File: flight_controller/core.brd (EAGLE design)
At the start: 96 x 48 mm, 119 parts, among them J1 M02, J10 M02, J11 M03, J12 M02, J13 M02, J14 M02, J15 M03, J16 M03, J17 M03, J18 M04, J19 M04, J2 M02, J20 M03, J21 M04, J3 M02, J4 M03, J5 M02, J6 M02, J7 M02, J8 M02, J9 M03, Q1 EM6K1, Q2 EM6K1, Q3 EM6K1, Q4 EM6K1, Q5 EM6K1, Q6 EM6K1, Q7 MOSFET-PCHANNEL-AON6407, U1 STM32F405, U2 MEAS-MS5611, U3 MPU-9250-QFN-24-NP, U4 MIC5219 3.3V, U5 USD-SOCKETNEW, Y1 16MHz

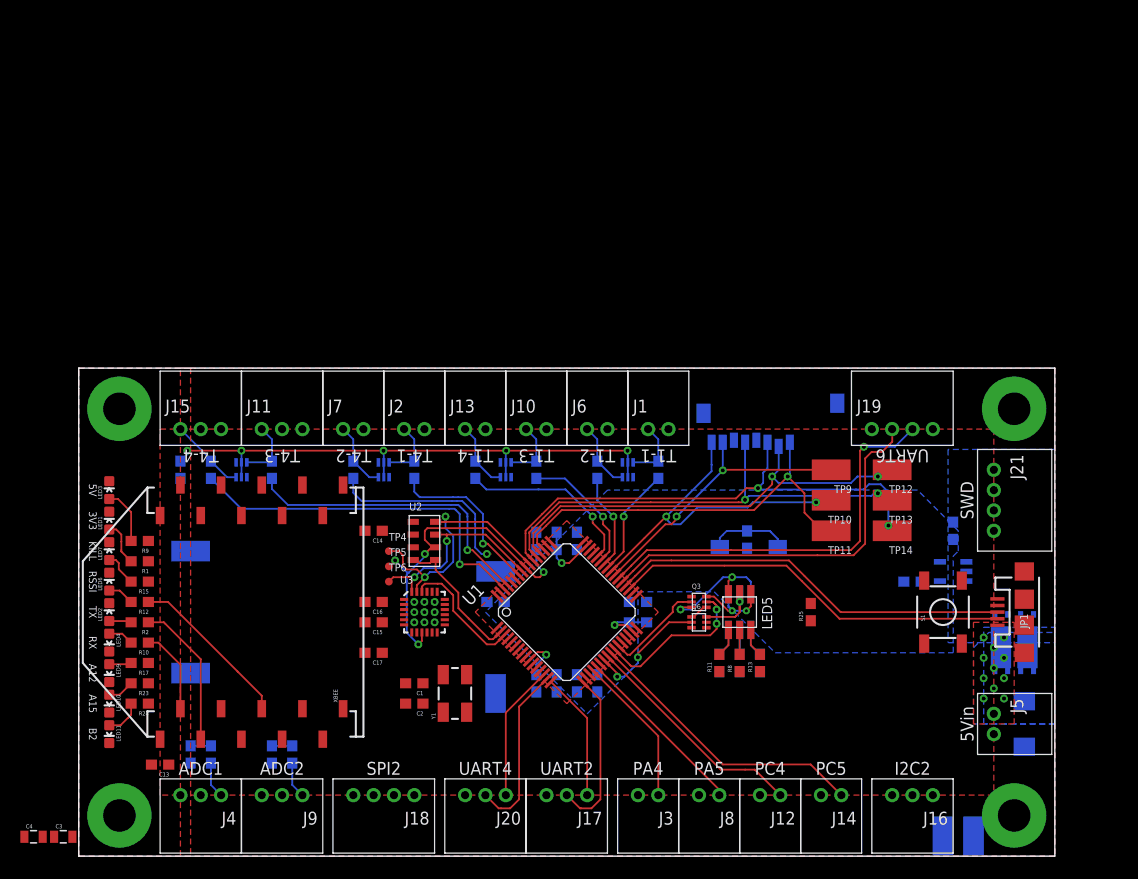
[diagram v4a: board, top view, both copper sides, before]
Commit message: Layout 70% done with new 8MHz crystal.
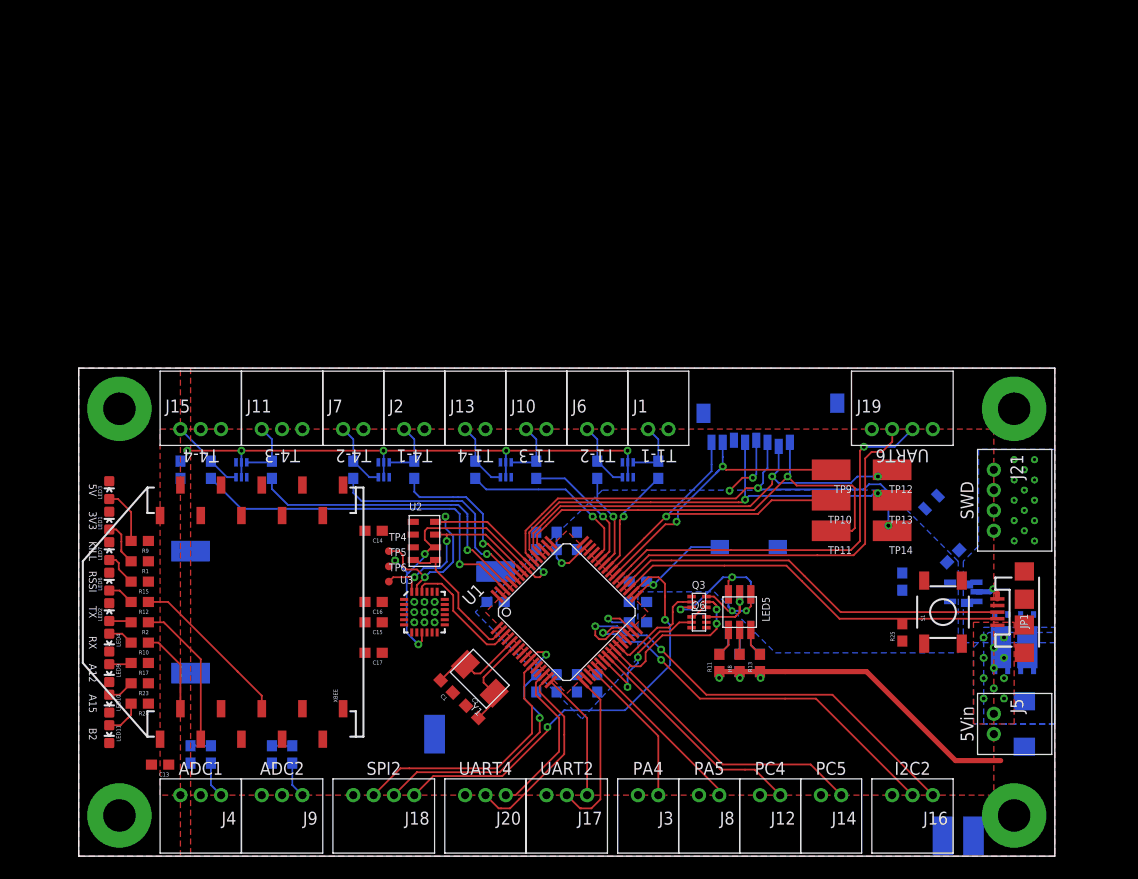
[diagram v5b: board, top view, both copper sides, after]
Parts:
- C4: value 10uF -> 1nF; device OSURC_Passives:0805 -> OSURC_Passives:0603
- C5: value 1nF -> 10uF; device OSURC_Passives:0603 -> OSURC_Passives:0805
- Y1: value 16MHz -> 8MHz; device SparkFun-FreqCtrl:CRYSTAL-SMD-5X3 -> OSURC_FreqCtrl:CX532
- moved C3 92.0 mm to (87.4, 25.8), flipped to the bottom, turned to 90 degrees
- moved C4 89.1 mm to (81.0, 27.0), flipped to the bottom, turned to 270 degrees
- moved R34 11.5 mm to (55.0, 27.0), turned to 0 degrees
- moved R25 9.22 mm to (81.0, 22.0)
- moved C5 8.03 mm to (83.9, 34.8), turned to 315 degrees
- moved TP15 7.21 mm to (35.0, 12.0)
- moved C2 5.75 mm to (38.7, 14.2), turned to 315 degrees
- moved C1 3.21 mm to (36.2, 16.7), turned to 135 degrees
- moved Y1 2.84 mm to (39.4, 17.4), turned to 135 degrees
- moved C6 2.50 mm to (86.0, 29.5), turned to 315 degrees
- moved U4 2.24 mm to (87.0, 26.0)
- turned C12 to 0 degrees
- turned C9 to 0 degrees
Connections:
- net 3.3V: now also C5.2; no longer C4.2
- net MIC-BP: now also C4.2; no longer C5.2
- net OSC-IN: now also Y1.2; no longer Y1.3
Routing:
- net I2C2-SCL: track 0.00 -> 44.7 mm, vias 0 -> 2
- net SPI2-SCK: track 0.00 -> 42.9 mm, vias 0 -> 2
- net I2C2-SDA: track 0.00 -> 40.2 mm, vias 0 -> 2
- net 5V: track 0.00 -> 31.3 mm, vias 0 -> 14
- net SPI2-MOSI: track 0.00 -> 25.6 mm
- net SPI2-MISO: track 4.45 -> 28.1 mm, vias 1 -> 2
- net OSC-OUT: track 0.00 -> 9.45 mm
- net OSC-IN: track 0.00 -> 9.25 mm
- net 3.3V: track 0.00 -> 6.64 mm, vias 9 -> 11
- net SDIO-D2: track 39.8 -> 45.6 mm
- net TIM4-CH2: track 19.4 -> 23.1 mm
- net USD-CD: track 8.01 -> 11.1 mm, vias 0 -> 1
- net GND: track 1.85 -> 4.75 mm, vias 0 -> 1
- net UART4-TX: track 13.4 -> 15.9 mm
- net UART4-RX: track 17.3 -> 19.3 mm
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
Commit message: FC layout 90% done.
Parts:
- removed TP15: TEST-POINT-KEYSTONE-5019, OSURC_Passives:PAD.15X.08
- TP1, TP7, TP8: value TEST-POINT-KEYSTONE-5019 -> TEST-POINT-PAD.03C; device OSURC_Passives:PAD.15X.08 -> OSURC_Passives:PAD-.03C
- moved TP8 22.7 mm to (88.0, 24.5), flipped to the top, turned to 0 degrees
- moved TP7 21.0 mm to (88.0, 23.0), flipped to the top, turned to 0 degrees
- moved TP9 20.6 mm to (58.0, 51.0), turned to 0 degrees
- moved TP11 20.6 mm to (66.0, 51.0), turned to 0 degrees
- moved TP10 20.0 mm to (62.0, 51.0), turned to 0 degrees
- moved TP14 19.1 mm to (78.0, 51.0), turned to 0 degrees
- moved TP13 17.1 mm to (74.0, 51.0), turned to 0 degrees
- moved TP12 16.4 mm to (70.0, 51.0), turned to 0 degrees
- moved S1 11.0 mm to (84.0, 35.0), turned to 0 degrees
- moved R25 9.85 mm to (85.0, 31.0), turned to 0 degrees
- moved C4 8.25 mm to (89.0, 29.0), flipped to the top, turned to 90 degrees
- moved C5 6.90 mm to (85.0, 28.0), turned to 90 degrees
- moved U4 5.83 mm to (92.0, 29.0)
- moved C3 4.84 mm to (91.0, 29.0), flipped to the top
- moved TP1 4.34 mm to (44.2, 25.1)
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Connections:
- net OSC-IN: no longer TP15.1
- net VIN: now also Q7.10, Q7.9
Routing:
- net PB2: track 0.00 -> 60.6 mm, vias 0 -> 6
- net PA12: track 0.00 -> 55.7 mm, vias 0 -> 4
- net PA15: track 0.00 -> 52.7 mm, vias 0 -> 4
- net 3.3V: track 6.64 -> 56.2 mm, vias 11 -> 12
- net SWDIO: track 0.00 -> 48.9 mm, vias 0 -> 4
- net SWCLK: track 0.00 -> 48.5 mm, vias 0 -> 4
- net TIM3-CH1-RSSI: track 16.3 -> 64.0 mm, vias 0 -> 5
- net UART2-RX-XBEE: track 24.9 -> 70.4 mm, vias 0 -> 1
- net UART2-TX-XBEE: track 27.1 -> 68.7 mm, vias 0 -> 1
- net ADC1: track 2.00 -> 42.3 mm, vias 0 -> 3
- net ADC2: track 2.00 -> 35.6 mm, vias 0 -> 3
- net GND: track 4.75 -> 25.7 mm, vias 1 -> 32
- net KILL: track 55.1 -> 72.8 mm, vias 5 -> 8
- net SDIO-D1: track 33.6 -> 17.6 mm
- net SDIO-CMD: track 50.1 -> 35.5 mm, vias 2 -> 1
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- added copper zone on layer 1, net MPU9250-REGOUT

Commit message: Resolve all errors and finish routing.
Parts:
- C13: value 100nF -> 10uF; device OSURC_Passives:0603 -> OSURC_Passives:0805
- moved TP9 20.6 mm to (73.5, 37.5)
- moved TP14 15.7 mm to (63.5, 45.0), turned to 90 degrees
- moved TP10 15.6 mm to (73.5, 40.5)
- moved C3 14.1 mm to (93.0, 15.0), turned to 0 degrees
- moved TP13 9.60 mm to (66.5, 45.0), turned to 90 degrees
- moved TP11 8.85 mm to (72.5, 45.0), turned to 90 degrees
- moved TP12 6.02 mm to (69.5, 45.0), turned to 90 degrees
- moved TP1 3.28 mm to (42.0, 27.5)
- moved C13 2.50 mm to (10.5, 9.00)
- moved R25 2.24 mm to (87.0, 32.0), flipped to the bottom, turned to 270 degrees
- moved C4 1.00 mm to (89.0, 28.0)
- moved D1 0.50 mm to (92.0, 17.5)
- turned C11 to 270 degrees
- turned C7 to 180 degrees
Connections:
- net 3.3V: now also C7.2; no longer C7.1
- net GND: now also C7.1; no longer C7.2
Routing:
- net 3.3V: track 56.2 -> 125.9 mm, vias 12 -> 45
- net RST: track 6.22 -> 63.1 mm, vias 1 -> 4
- net SDIO-D1: track 17.6 -> 34.1 mm
- net USD-CD: track 16.8 -> 32.3 mm, vias 1 -> 2
- net SDIO-D0: track 18.9 -> 31.6 mm
- net SDIO-CK: track 32.6 -> 43.1 mm
- net SDIO-D2: track 35.9 -> 46.1 mm
- net SDIO-D3: track 34.9 -> 43.1 mm
- net SDIO-CMD: track 35.5 -> 41.7 mm
- net 5V: track 30.6 -> 35.7 mm, vias 25 -> 23
- net UART2-RX-XBEE: track 70.4 -> 74.3 mm, vias 1 -> 2
- net F4-VCAP-1: track 5.95 -> 3.84 mm
- net MIC-BP: track 0.00 -> 2.03 mm, vias 0 -> 1
- net UART4-TX: track 15.9 -> 17.3 mm
- net UART4-RX: track 19.3 -> 20.2 mm
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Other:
- board text added: "CK"
- board text added: "CMD"
- board text added: "D0"
- board text added: "D1"
- board text added: "D2"
- board text added: "D3"

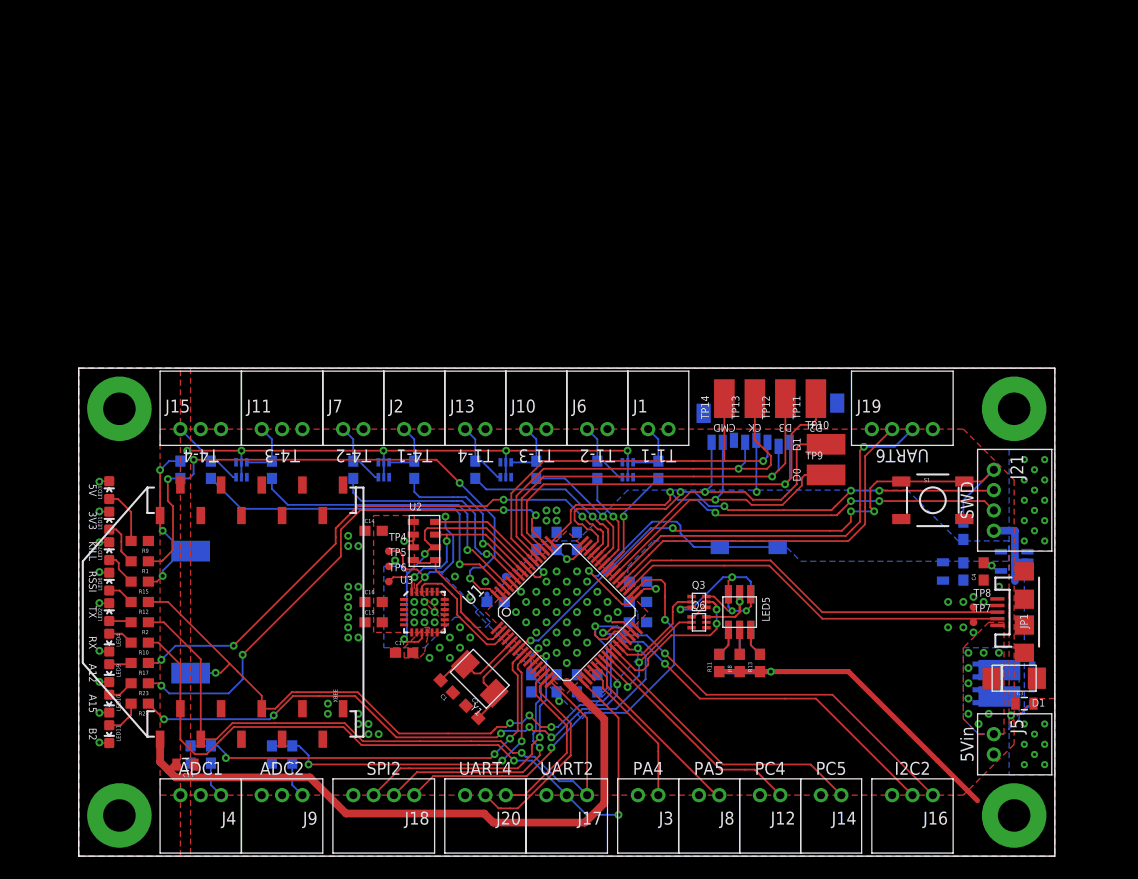
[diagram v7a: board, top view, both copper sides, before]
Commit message: Add USB diffpair net class and USB termination resistors.
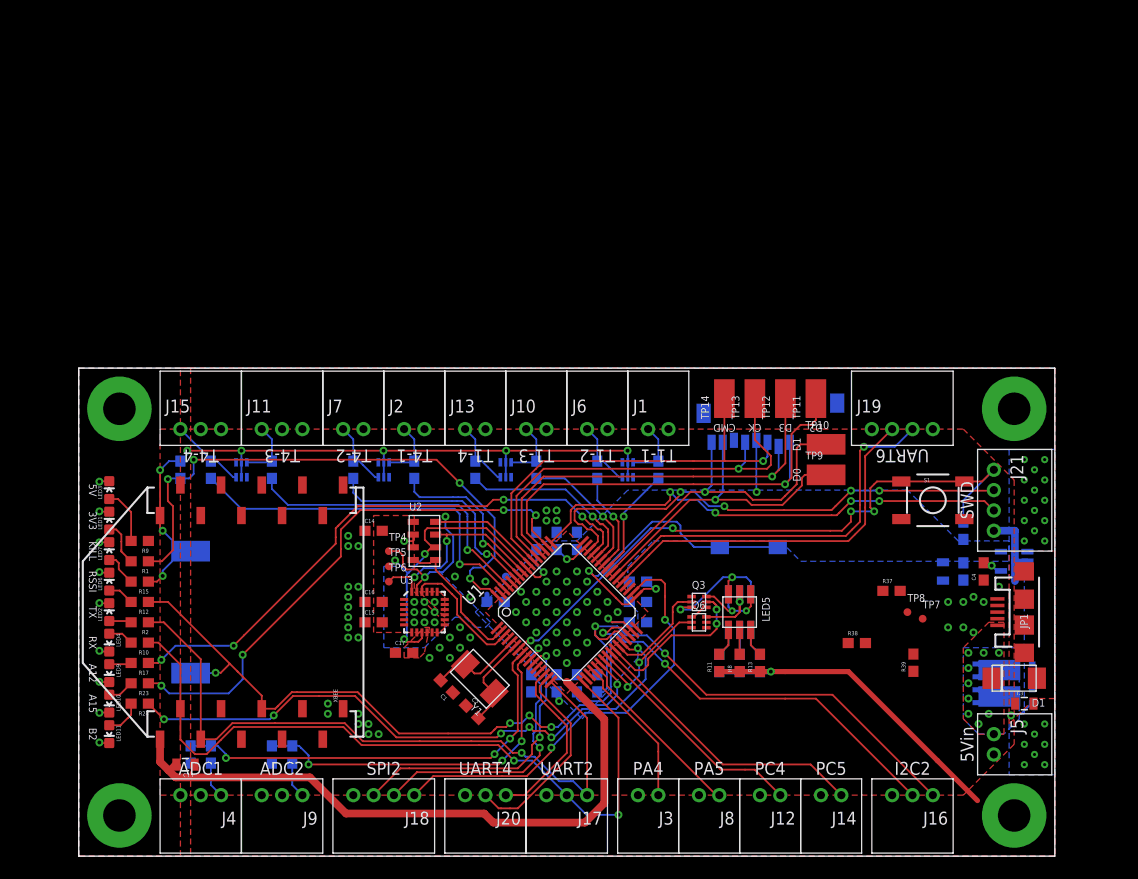
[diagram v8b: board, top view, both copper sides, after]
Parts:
- added R37: 1.5k, OSURC_Passives:0603
- added R38, R39: 22, OSURC_Passives:0603
- moved TP8 6.52 mm to (81.5, 24.0)
- moved TP7 5.01 mm to (83.0, 23.4)
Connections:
- removed net OTG-HS-DM: JP1.D-, TP7.1, U1.35
- removed net OTG-HS-DP: JP1.D+, TP8.1, U1.36
- new net OTG-HS-D'_N: R39.1, U1.35
- new net OTG-HS-D'_P: R37.1, R38.1, U1.36
- new net OTG-HS-D_N: JP1.D-, R39.2, TP7.1
- new net OTG-HS-D_P: JP1.D+, R38.2, TP8.1
- net 3.3V: now also R37.2
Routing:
- net OTG-HS-DP: track 40.2 -> 0.00 mm
- net OTG-HS-DM: track 39.7 -> 0.00 mm
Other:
- outline, holes or cut-outs redrawn
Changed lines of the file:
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@@
 <?xml version="1.0" encoding="utf-8"?>
 <!DOCTYPE eagle SYSTEM "eagle.dtd">
-<eagle version="7.1.0">
+<eagle version="7.2.0">
 <drawing>
 <settings>
@@
 <setting verticaltext="up"/>
 </settings>
-<grid distance="0.005" unitdist="inch" unit="inch" style="lines" multiple="1" display="yes" altdistance="0.025" altunitdist="inch" altunit="inch"/>
+<grid distance="0.5" unitdist="mm" unit="mm" style="lines" multiple="1" display="yes" altdistance="0.025" altunitdist="inch" altunit="inch"/>
 <layers>
 <layer number="1" name="Top" color="4" fill="1" visible="yes" active="yes"/>
@@
 <board>
 <plain>
-<wire x1="0" y1="0" x2="0" y2="46" width="0.05" layer="20"/>
-<wire x1="0" y1="46" x2="0" y2="48" width="0.05" layer="20"/>
+<wire x1="0" y1="0" x2="0" y2="48" width="0.05" layer="20"/>
 <wire x1="0" y1="48" x2="96" y2="48" width="0.05" layer="20"/>
 <wire x1="96" y1="48" x2="96" y2="0" width="0.05" layer="20"/>
@@
 <classes>
 <class number="0" name="default" width="0" drill="0">
+</class>
+<class number="1" name="USB" width="0.6096" drill="0">
 </class>
 </classes>
@@
 <attribute name="DIGIKEY_PN" value="5019KCT-ND" x="11" y="18" size="1.778" layer="28" rot="MR0" display="off"/>
 </element>
-<element name="TP7" library="OSURC_Passives" package="PAD-.03C" value="TEST-POINT-PAD.03C" x="88" y="23"/>
-<element name="TP8" library="OSURC_Passives" package="PAD-.03C" value="TEST-POINT-PAD.03C" x="88" y="24.5"/>
+<element name="TP7" library="OSURC_Passives" package="PAD-.03C" value="TEST-POINT-PAD.03C" x="83" y="23.35"/>
+<element name="TP8" library="OSURC_Passives" package="PAD-.03C" value="TEST-POINT-PAD.03C" x="81.5" y="24"/>
 <element name="TP9" library="OSURC_Passives" package="PAD.15X.08" value="TEST-POINT-KEYSTONE-5019" x="73.5" y="37.5">
 <attribute name="DIGIKEY_PN" value="5019KCT-ND" x="73.5" y="37.5" size="1.778" layer="27" display="off"/>
@@
 <element name="C5" library="OSURC_Passives" package="0805" value="10uF" x="85" y="28" rot="MR90">
 <attribute name="DIGIKEY_PN" value="490-1709-1-ND" x="85" y="28" size="1.27" layer="28" rot="MR90" display="off"/>
+</element>
+<element name="R37" library="OSURC_Passives" package="0603" value="1.5k" x="79.938" y="26.09">
+<attribute name="DIGIKEY_PN" value="P1.5KGCT-ND" x="79.938" y="26.09" size="1.778" layer="27" display="off"/>
+</element>
+<element name="R38" library="OSURC_Passives" package="0603" value="22" x="76.524" y="20.959">
+<attribute name="DIGIKEY_PN" value="P22GCT-ND" x="76.524" y="20.959" size="1.778" layer="27" display="off"/>
+</element>
+<element name="R39" library="OSURC_Passives" package="0603" value="22" x="82.089" y="19.024" rot="R90">
+<attribute name="DIGIKEY_PN" value="P22GCT-ND" x="82.089" y="19.024" size="1.778" layer="27" rot="R90" display="off"/>
 </element>
 </elements>
@@
 <wire x1="11.303" y1="37.592" x2="11.303" y2="38.989" width="0.1778" layer="16"/>
 <via x="11.303" y="38.989" extent="1-16" drill="0.381"/>
-<wire x1="11.303" y1="38.989" x2="35.052" y2="38.989" width="0.1778" layer="1"/>
-<wire x1="35.052" y1="38.989" x2="35.179" y2="38.989" width="0.1778" layer="1"/>
+<wire x1="11.303" y1="38.989" x2="35.179" y2="38.989" width="0.1778" layer="1"/>
 <wire x1="35.179" y1="38.989" x2="37.465" y2="36.703" width="0.1778" layer="1"/>
 <via x="37.465" y="36.703" extent="1-16" drill="0.381"/>
@@
 <wire x1="8.763" y1="34.925" x2="9.271" y2="34.417" width="0.1778" layer="1"/>
 <wire x1="9.271" y1="34.417" x2="9.271" y2="30.099" width="0.1778" layer="1"/>
-<wire x1="9.271" y1="30.099" x2="8.255" y2="29.083" width="0.1778" layer="1"/>
-<wire x1="8.255" y1="29.083" x2="8.172" y2="29" width="0.1778" layer="1"/>
+<wire x1="9.271" y1="30.099" x2="8.172" y2="29" width="0.1778" layer="1"/>
 <wire x1="8.172" y1="29" x2="6.85" y2="29" width="0.1778" layer="1"/>
 <polygon width="0.1778" layer="16" rank="2">
@@
 <wire x1="9.381" y1="9" x2="8.8265" y2="8.4455" width="0.508" layer="1"/>
 <contactref element="C7" pad="2"/>
+<contactref element="R37" pad="2"/>
+<wire x1="85" y1="28.9" x2="80.788" y2="26.09" width="0" layer="19" extent="1-16"/>
 </signal>
 <signal name="KILL">
@@
 <wire x1="46.482" y1="10.668" x2="49.784" y2="14.097" width="0.1778" layer="16"/>
 </signal>
-<signal name="OTG-HS-DP">
-<contactref element="U1" pad="36"/>
-<contactref element="JP1" pad="D+"/>
-<contactref element="TP8" pad="1"/>
-<wire x1="53.798275" y1="26.61629375" x2="54.74098125" y2="27.559" width="0.1778" layer="1"/>
-<wire x1="68.042" y1="29.083" x2="73.125" y2="24" width="0.1778" layer="1"/>
-<wire x1="73.125" y1="24" x2="88" y2="24" width="0.1778" layer="1"/>
-<wire x1="88" y1="24" x2="90.35" y2="24" width="0.1778" layer="1"/>
-<wire x1="68.042" y1="29.083" x2="58.293" y2="29.083" width="0.1778" layer="1"/>
-<wire x1="58.293" y1="29.083" x2="56.26498125" y2="29.083" width="0.1778" layer="1"/>
-<wire x1="56.26498125" y1="29.083" x2="54.74098125" y2="27.559" width="0.1778" layer="1"/>
-<wire x1="88" y1="24.5" x2="88" y2="24" width="0.1778" layer="1"/>
-</signal>
 <signal name="SPI1-MISO">
 <contactref element="U1" pad="56"/>
@@
 <wire x1="33.75" y1="21.431" x2="33.401" y2="21.082" width="0.1778" layer="1"/>
 <wire x1="33.401" y1="21.082" x2="33.02" y2="21.082" width="0.1778" layer="1"/>
-</signal>
-<signal name="OTG-HS-DM">
-<contactref element="U1" pad="35"/>
-<contactref element="JP1" pad="D-"/>
-<contactref element="TP7" pad="1"/>
-<wire x1="54.151828125" y1="26.262740625" x2="54.9400875" y2="27.051" width="0.1778" layer="1"/>
-<wire x1="67.915" y1="28.575" x2="73.14" y2="23.35" width="0.1778" layer="1"/>
-<wire x1="73.14" y1="23.35" x2="88" y2="23.35" width="0.1778" layer="1"/>
-<wire x1="88" y1="23.35" x2="90.35" y2="23.35" width="0.1778" layer="1"/>
-<wire x1="67.915" y1="28.575" x2="63.5" y2="28.575" width="0.1778" layer="1"/>
-<wire x1="63.5" y1="28.575" x2="56.4640875" y2="28.575" width="0.1778" layer="1"/>
-<wire x1="56.4640875" y1="28.575" x2="54.9400875" y2="27.051" width="0.1778" layer="1"/>
-<wire x1="88" y1="23" x2="88" y2="23.35" width="0.1778" layer="1"/>
 </signal>
 <signal name="SPI2-MISO">
@@
 <wire x1="43.5" y1="26" x2="42" y2="27.5" width="0.1778" layer="16"/>
 </signal>
+<signal name="OTG-HS-D_N" class="1">
+<contactref element="JP1" pad="D-"/>
+<contactref element="TP7" pad="1"/>
+<contactref element="R39" pad="2"/>
+<wire x1="83" y1="23.35" x2="90.35" y2="23.35" width="0" layer="19" extent="1-1"/>
+<wire x1="82.089" y1="19.874" x2="83" y2="23.35" width="0" layer="19" extent="1-1"/>
+</signal>
+<signal name="OTG-HS-D_P" class="1">
+<contactref element="JP1" pad="D+"/>
+<contactref element="TP8" pad="1"/>
+<contactref element="R38" pad="2"/>
+<wire x1="81.5" y1="24" x2="90.35" y2="24" width="0" layer="19" extent="1-1"/>
+<wire x1="77.374" y1="20.959" x2="81.5" y2="24" width="0" layer="19" extent="1-1"/>
+</signal>
+<signal name="OTG-HS-D'_N" class="1">
+<contactref element="U1" pad="35"/>
+<contactref element="R39" pad="1"/>
+<wire x1="54.151828125" y1="26.262740625" x2="82.089" y2="18.174" width="0" layer="19" extent="1-1"/>
+</signal>
+<signal name="OTG-HS-D'_P" class="1">
+<contactref element="U1" pad="36"/>
+<contactref element="R37" pad="1"/>
+<contactref element="R38" pad="1"/>
+<wire x1="75.674" y1="20.959" x2="79.088" y2="26.09" width="0" layer="19" extent="1-1"/>
+<wire x1="53.798275" y1="26.61629375" x2="75.674" y2="20.959" width="0" layer="19" extent="1-1"/>
+</signal>
 </signals>
